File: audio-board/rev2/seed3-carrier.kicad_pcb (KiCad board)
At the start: 4 copper layers, 90 x 56.5 mm, 59 parts, among them J1 AudioJack2_Switch, J2 AudioJack2, J3 POWER_BOARD, J4 DISPLAY_UART, J5 SJ3-35063AG, J8 LINE_OUT, J9 SJ3-35063AG, Q1 AO3401A, Q4 2N7002, U1 TLV9064IDR, U2 TPA6132A2RTE

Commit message: Isolate HP_EN from U2 and fix the AUX and line-out levels
The Daisy can run from USB while the carrier's +5V is off. HP_EN then
drove U2's EN pin above its VDD + 0.3 V rating. U4 (TXU0101) now sits
between HP_EN and EN, powered from the Daisy's 3V3_D and +5V. Its
output goes high-impedance when either supply is off, and R26 holds
EN low.

- R38 47k -> 4.7k: with the same signal on both AUX channels, 2 Vrms
  reached the Daisy at 4.9 Vpp, over its 3.6 Vpp range. Now 2.7 Vpp.
- R43 1k -> 10k: limits current into an unpowered display. Caps the
  display UART at 230400 baud.
- Speaker enable delay raised from 0.5 s to 4 s after power-on, so the
  line-out bias settles before the speaker amp unmutes.
- DESIGN.md, CHANGES.md and TEST_PLAN.md updated to match.

Co-Authored-By: Claude Opus 5.5 <noreply@anthropic.com>
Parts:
- added C37: 100nF, Capacitor_SMD:C_1206_3216Metric_Pad1.33x1.80mm_HandSolder, F.Cu at (157.6, 80.6)
- added C38: 100nF, Capacitor_SMD:C_1206_3216Metric_Pad1.33x1.80mm_HandSolder, F.Cu at (161.4, 76.4)
- added U4: TXU0101, Package_TO_SOT_SMD:SOT-23-6, F.Cu at (161.4, 80.6)
- R38: value 47k -> 4.7k
- R43: value 1k -> 10k
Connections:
- A1 pad 38: unconnected-(A1-3V3_D-Pad38) -> /3V3_D
- R26 pad 1: /HP_EN -> /U2_EN
- U2 pad 13: /HP_EN -> /U2_EN

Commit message: Place the SOIC-8 U1, C8 and the line-out filter
U1 takes the old SOIC-14 spot with pin 3 next to R1 and both outputs
heading straight to Daisy pins 16 and 17. C8 sits above pin 8. R28/C24
move beside J8 so the long run from the Daisy carries the low-impedance
DAC output. Includes the Update PCB from Schematic sync for U1's new
footprint and the removed line-out buffer parts.

Co-Authored-By: Claude Opus 5.5 <noreply@anthropic.com>
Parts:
- removed C25: 1uF, Capacitor_SMD:C_1206_3216Metric_Pad1.33x1.80mm_HandSolder
- removed C26: 10uF 16V, Capacitor_SMD:C_1206_3216Metric_Pad1.33x1.80mm_HandSolder
- removed R29: 1M, Resistor_SMD:R_1206_3216Metric_Pad1.30x1.75mm_HandSolder
- removed R3: 100, Resistor_SMD:R_1206_3216Metric_Pad1.30x1.75mm_HandSolder
- U1: value TLV9064IDR -> TLV9062IDR; footprint Package_SO:SOIC-14_3.9x8.7mm_P1.27mm -> Package_SO:SOIC-8_3.9x4.9mm_P1.27mm
- moved C24 20.2 mm to (168.0, 72.6)
- moved R28 13.9 mm to (162.6, 72.6), turned to 0 degrees
- moved C8 10.2 mm to (140.0, 84.5), turned to -90 degrees
- moved U1 2.00 mm to (137.0, 90.0), turned to 0 degrees
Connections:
- C24 pad 1: Net-(C24-Pad1) -> /LINE_OUT
- C32 pad 2: Net-(U1D-+) -> Net-(U1B-+)
- R28 pad 2: Net-(C24-Pad1) -> /LINE_OUT
- R39 pad 2: Net-(U1D-+) -> Net-(U1B-+)
- U1 pad 4: +5V -> GND
- U1 pad 5: /VREF -> Net-(U1B-+)
- U1 pad 6: Net-(U1B--) -> /AUDIO_IN_2
- U1 pad 7: Net-(U1B--) -> /AUDIO_IN_2
- U1 pad 8: Net-(U1C--) -> +5V

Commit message: Feed the AUX input straight to the Daisy and use a single op-amp
The Seed3's inputs are AC-coupled and the TAC5242 presents about 5k,
so the R40/R41 sum can drive Daisy pin 17 directly. This drops U1B,
C32 and R39, and R38 becomes a 100k DC return. U1 is now a TLV9061 in
SOT-23-5, with a two-unit project symbol, re-placed at the end of the
guitar row with C8 beside its V+ pin. TEST_PLAN 5.17 checks the AUX
level with the Daisy fitted.

Co-Authored-By: Claude Opus 5.5 <noreply@anthropic.com>
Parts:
- removed C32: 1uF, Capacitor_SMD:C_1206_3216Metric_Pad1.33x1.80mm_HandSolder
- removed R39: 100k, Resistor_SMD:R_1206_3216Metric_Pad1.30x1.75mm_HandSolder
- R38: value 4.7k -> 100k
- U1: value TLV9062IDR -> TLV9061IDBVR; footprint Package_SO:SOIC-8_3.9x4.9mm_P1.27mm -> Package_TO_SOT_SMD:SOT-23-5
- moved C8 6.70 mm to (140.1, 91.2), turned to 180 degrees
- moved U1 2.62 mm to (135.5, 92.2)
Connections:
- C31 pad 1: Net-(C31-Pad1) -> /AUDIO_IN_2
- R38 pad 1: Net-(C31-Pad1) -> /AUDIO_IN_2
- R40 pad 2: Net-(C31-Pad1) -> /AUDIO_IN_2
- R41 pad 2: Net-(C31-Pad1) -> /AUDIO_IN_2
- U1 pad 2: /AUDIO_IN_1 -> GND
- U1 pad 4: GND -> /AUDIO_IN_1
- U1 pad 5: Net-(U1B-+) -> +5V

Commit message: Remove U4, C37, C38 and R26 and tie U2 EN to +5V
The codec already powers down its DAC when an IWDG reset stops its
clocks, which silences the headphones as well as J2. Driving U2's EN
from the Daisy needed a level translator because the Daisy can run
from USB with +5V off, so drop it and leave U2 always on.

Co-Authored-By: Claude Opus 5.5 <noreply@anthropic.com>
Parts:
- removed C37, C38: 100nF, Capacitor_SMD:C_1206_3216Metric_Pad1.33x1.80mm_HandSolder
- removed R26: 100k, Resistor_SMD:R_1206_3216Metric_Pad1.30x1.75mm_HandSolder
- removed U4: TXU0101, Package_TO_SOT_SMD:SOT-23-6
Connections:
- A1 pad 33: /HP_EN -> unconnected-(A1-SAI2_SD_A-Pad33)
- A1 pad 38: /3V3_D -> unconnected-(A1-3V3_D-Pad38)
- U2 pad 13: /U2_EN -> +5V

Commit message: Add a +5V sense on Daisy pin 22 to keep USB-only audio out of U2
With the Daisy on USB and +5V off, U2's charge pump rails sit at 0 V,
so its inputs are rated only to about +-0.3 V, while C12/C13 pass pin
18's full-scale +-1.4 V. R45/R46 (100k/100k) put +5V/2 on 5V_SENSE
(ADC_0) so the firmware can hold the outputs silent while +5V is down.

DESIGN.md sets the firmware thresholds and settle time and notes the
fast-power-loss limit; TEST_PLAN 5.18 scopes the transitions.

Co-Authored-By: Claude Opus 5.5 <noreply@anthropic.com>
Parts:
- added R45: 100k, Resistor_SMD:R_1206_3216Metric_Pad1.30x1.75mm_HandSolder, F.Cu at (163.6, 66.6)
- added R46: 100k, Resistor_SMD:R_1206_3216Metric_Pad1.30x1.75mm_HandSolder, F.Cu at (166.6, 66.6)
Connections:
- A1 pad 22: unconnected-(A1-ADC_0-Pad22) -> /5V_SENSE

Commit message: Re-lay out the carrier schematic into framed functional sections
Group the sheet into eleven dashed, titled sections laid out left to
right (inputs and supply, Daisy and display, outputs, power board and
mute), moving each block rigidly so no connection changes. Misplaced
parts move to their own blocks: the AUX input, C17/C18, FB1/C30, J2/J8.

Rewrite every note in one style inside its section, correct the stale
HP_DETECT/SPK_EN note, and add notes for the AUX input, VREF, display
resistors and Daisy sockets. Update the title block, set J1/J2 to
NRJ4HF and C7/C18 to the 16 V parts on the BOM (board values match).

Co-Authored-By: Claude Opus 5.5 <noreply@anthropic.com>
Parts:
- C18, C7: value 47uF 10V -> 47uF 16V
- J1: value AudioJack2_Switch -> NRJ4HF
- J2: value AudioJack2 -> NRJ4HF
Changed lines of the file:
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@@
 			)
 		)
-		(property "Value" "AudioJack2"
+		(property "Value" "NRJ4HF"
 			(at 6.35 15 270)
 			(layer "F.Fab")
@@
 			)
 		)
-		(property "Value" "AudioJack2_Switch"
+		(property "Value" "NRJ4HF"
 			(at 6.35 15 270)
 			(layer "F.Fab")
@@
 			)
 		)
-		(property "Value" "47uF 10V"
+		(property "Value" "47uF 16V"
 			(at 0 2.3 0)
 			(layer "F.Fab")
@@
 			)
 		)
-		(property "Value" "47uF 10V"
+		(property "Value" "47uF 16V"
 			(at 1 3.75 0)
 			(layer "F.Fab")

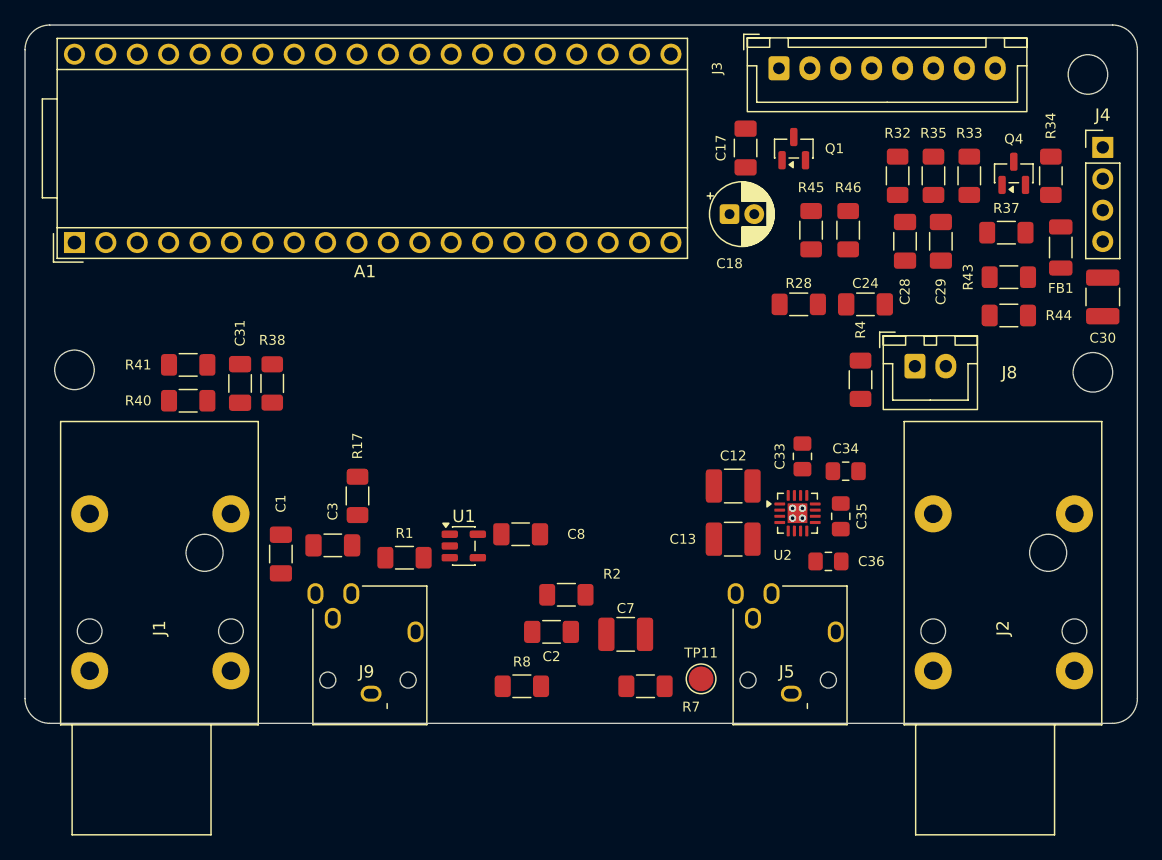
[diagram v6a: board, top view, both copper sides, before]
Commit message: Re-annotate the carrier board in sheet order
Renumber R, C, J, Q and TP left to right, then top to bottom by
section, so the designators have no gaps: R1-R19, C1-C18, J1-J7,
Q1-Q2, TP1. U1, U2, A1 and FB1 keep their numbers, so the U1/U2
design rules are unchanged.

Apply one mapping to the schematic, the board, the sheet notes and
DESIGN.md/TEST_PLAN.md, and rename the five auto-generated board nets
that embed a designator. CHANGES.md names removed parts by their rev 1
designator and lists every old number against its new one.

Netlists before and after match net for net once the old one is
translated through the mapping; ERC and schematic parity are clean.

Co-Authored-By: Claude Opus 5.5 <noreply@anthropic.com>
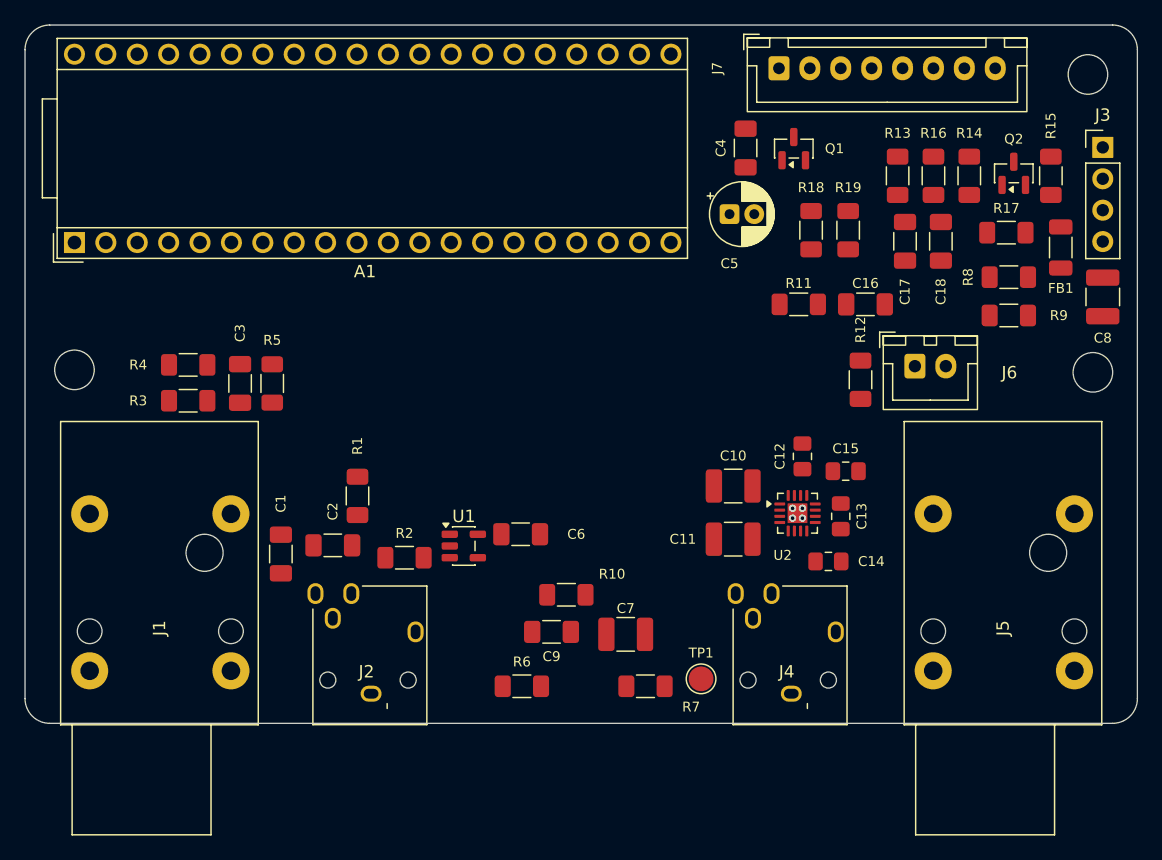
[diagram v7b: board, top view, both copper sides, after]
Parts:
- renumbered C12 to C10, C13 to C11, C33 to C12, C35 to C13, C36 to C14, C34 to C15, C24 to C16, C28 to C17, C29 to C18, C3 to C2, C31 to C3, C17 to C4, C18 to C5, C8 to C6, C30 to C8, C2 to C9, J9 to J2, J4 to J3, J5 to J4, J2 to J5, J8 to J6, J3 to J7, Q4 to Q2, R17 to R1, R2 to R10, R28 to R11, R4 to R12, R32 to R13, R33 to R14, R34 to R15, R35 to R16, R37 to R17, R45 to R18, R46 to R19, R1 to R2, R40 to R3, R41 to R4, R38 to R5, R8 to R6, R43 to R8, R44 to R9, TP11 to TP1

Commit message: Set R5 to 3.3k and run U2 at -6 dB
R5 at 100k left the AUX level to the Daisy's unpublished input
impedance: with no module load a 2 Vrms source would reach ~5.4 Vpp,
past the pin's absolute maximum. At 3.3k, R3||R4 into R5 alone caps it
at 2.25 Vpp, and the expected level is 1.5-1.7 Vpp.

At 0 dB, full scale (~0.75 Vrms) clips U2 into 16 ohm headphones: its
1% THD limit there is 25 mW (~0.63 Vrms). Tying G0 to GND gives -6 dB
and ~0.40 Vrms full scale, with 4-6 dB of margin at 16-32 ohm.

DESIGN.md, CHANGES.md, TEST_PLAN.md and the sheet notes carry the new
levels and corners.

Co-Authored-By: Claude Opus 5.5 <noreply@anthropic.com>
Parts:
- R5: value 100k -> 3.3k
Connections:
- U2 pad 6: +5V -> GND
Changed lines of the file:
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@@
 			)
 		)
-		(property "Value" "100k"
+		(property "Value" "3.3k"
 			(at 0 1.83 270)
 			(layer "F.Fab")
@@
 			)
 		)
-		(property "LCSC" "C17900"
+		(property "LCSC" "C26032"
 			(at 0 0 0)
 			(layer "F.Fab")
@@
 			(layers "F.Cu" "F.Mask" "F.Paste")
 			(roundrect_rratio 0.25)
-			(net "+5V")
+			(net "GND")
 			(pinfunction "G0_6")
 			(pintype "input")
